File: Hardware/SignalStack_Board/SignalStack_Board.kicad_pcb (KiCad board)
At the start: 2 copper layers, 101.6 x 76.2 mm, 68 parts, among them J1 Molex_uF_SV_06, J2 RJ45_LED_Shielded, J3 Molex_uF_SV_06, Q1 SI4156DY, Q2 SI4156DY, Q3 SI4156DY, Q4 SI4156DY, Q5 SI4156DY, Q6 SI4156DY, Q7 SI4156DY, Q8 SI4156DY, U1 OKI, U10 74LVC2G04, U2 SMAJ12CA, U3 Teensy4.1_DEV-16771, U4 TSR_1-2450, U5 IRS2005S, U6 IRS2005S, U7 74LVC2G04, U8 IRS2005S, U9 IRS2005S

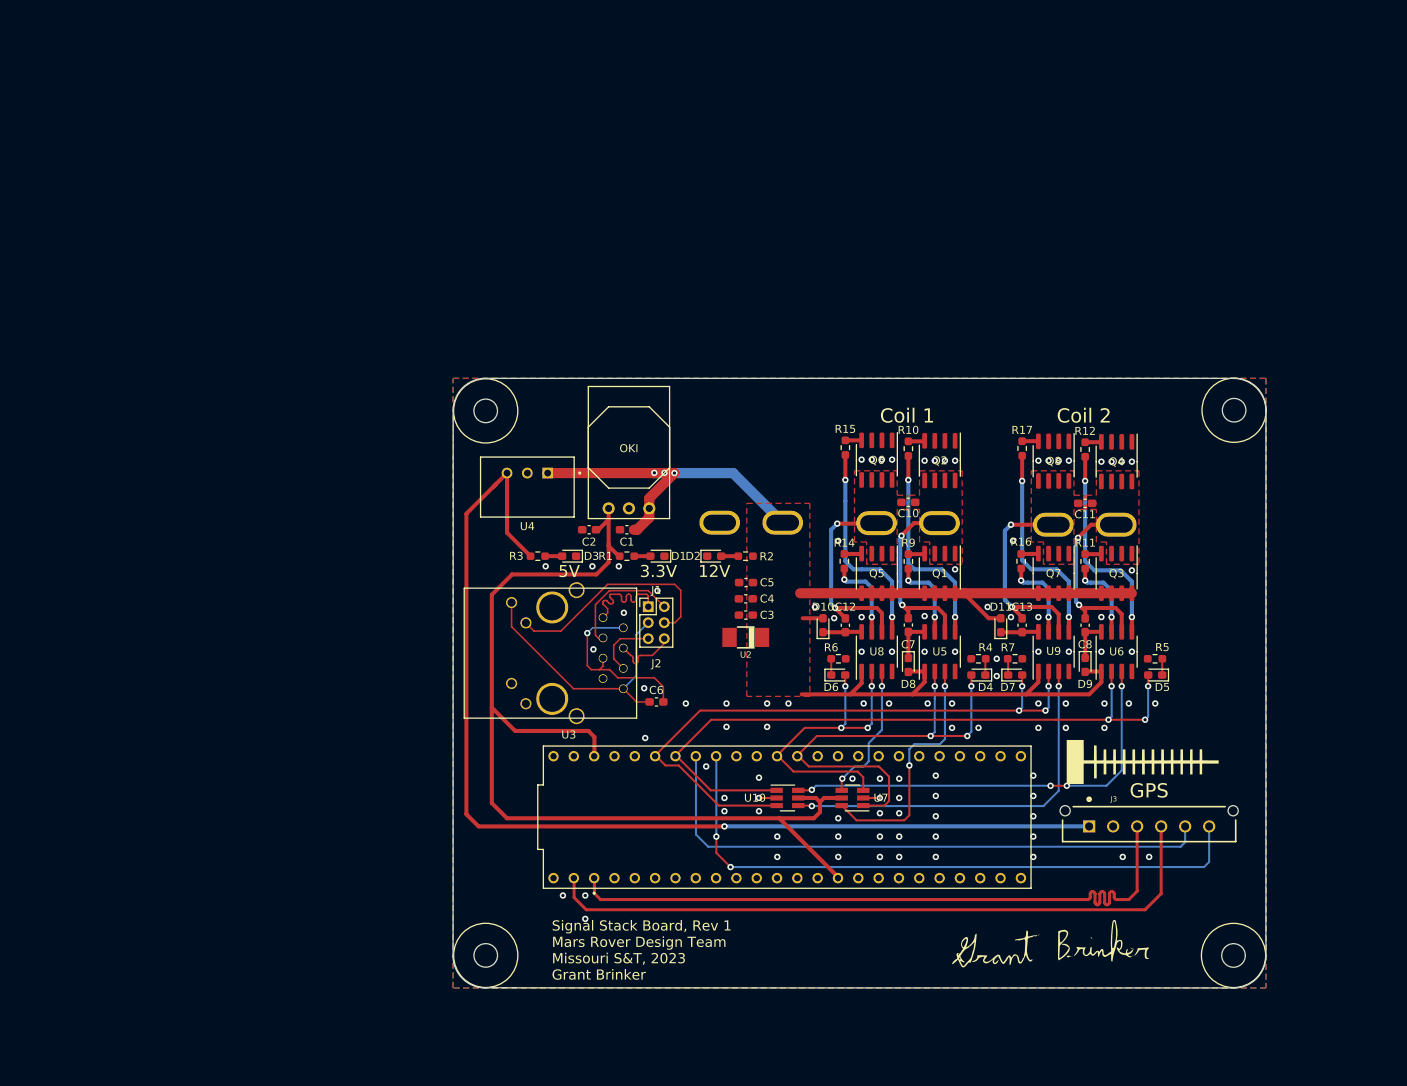
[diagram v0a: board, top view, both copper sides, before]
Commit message: Started layout
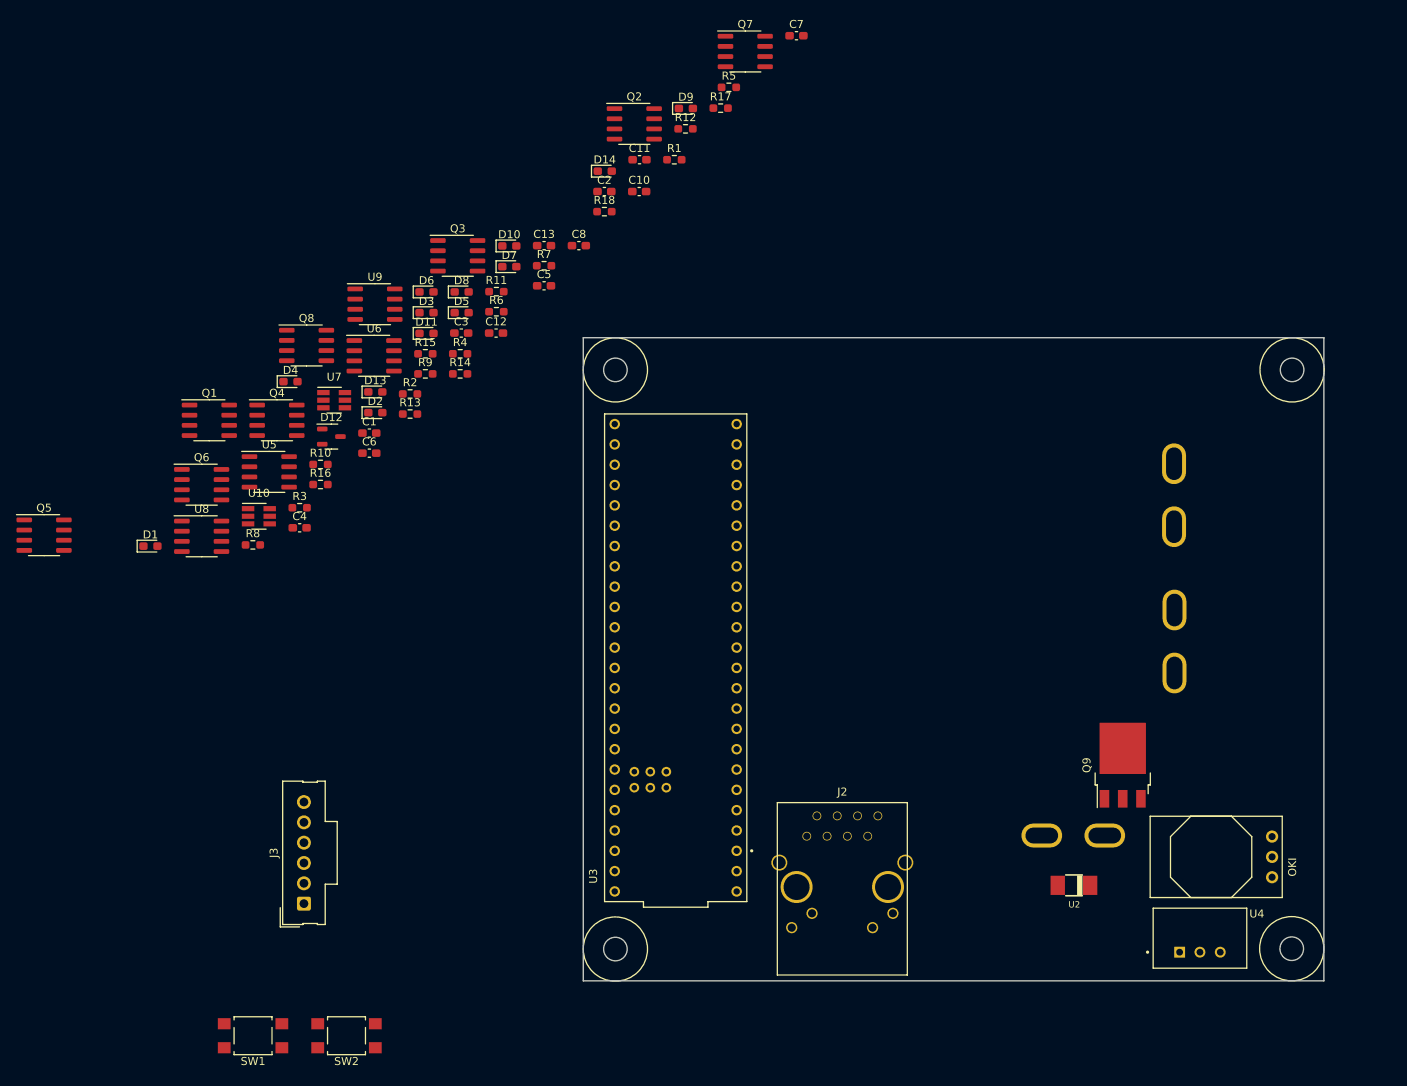
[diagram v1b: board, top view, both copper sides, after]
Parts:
- removed G***: LOGO, MRDT_Silkscreens:yagi
- removed G***: LOGO, MRDT_Silkscreens:z_sig_Grant_Brinker_25mmx6
- removed J1: Molex_uF_SV_06, Connector_PinHeader_2.00mm:PinHeader_2x03_P2.00mm_Vertical
- added D12: D_Zener, Package_TO_SOT_SMD:SOT-23-3, F.Cu at (80.9, 70.4)
- added D13: Blue, LED_SMD:LED_0603_1608Metric_Pad1.05x0.95mm_HandSolder, F.Cu at (86.4, 64.8)
- added D14: Blue, LED_SMD:LED_0603_1608Metric_Pad1.05x0.95mm_HandSolder, F.Cu at (115.1, 37.2)
- added Q9: Q_PMOS_DGS, Package_TO_SOT_SMD:TO-252-3_TabPin2, F.Cu at (179.8, 111.5)
- added R13: 120, Resistor_SMD:R_0603_1608Metric_Pad0.98x0.95mm_HandSolder, F.Cu at (90.8, 67.6)
- added R18: 120, Resistor_SMD:R_0603_1608Metric_Pad0.98x0.95mm_HandSolder, F.Cu at (115.0, 42.3)
- added R8: 100k, Resistor_SMD:R_0603_1608Metric_Pad0.98x0.95mm_HandSolder, F.Cu at (71.1, 83.9)
- added SW1: SW_Push, Button_Switch_SMD:SW_SPST_TL3305A, F.Cu at (71.1, 145.3)
- added SW2: SW_Push, Button_Switch_SMD:SW_SPST_TL3305A, F.Cu at (82.8, 145.3)
- Conn1: moved to F.Cu
- Conn2, Conn3: moved to B.Cu
- J3: footprint MRDT_Connectors:MOLEX_uF_S_06_Vertical -> Connector_Molex:Molex_SL_171971-0006_1x06_P2.54mm_Vertical
- U3: footprint MRDT_Shields:Teensy_4_1_Bare -> MRDT_Shields:Teensy_4_1_Ethernet
- moved V3 108.8 mm to (205.0, 138.4), turned to 90 degrees
- moved J3 106.1 mm to (77.5, 128.8), turned to 90 degrees
- moved Q4 105.1 mm to (74.1, 68.4), turned to 0 degrees
- moved Q5 104.2 mm to (45.0, 82.7), turned to 0 degrees
- moved V1 102.6 mm to (112.4, 138.5)
- moved U4 101.2 mm to (189.5, 133.1), turned to 0 degrees
- moved U6 99.9 mm to (86.3, 60.3), turned to 0 degrees
- moved D5 97.8 mm to (97.2, 54.9), turned to 0 degrees
- moved U9 95.3 mm to (86.4, 53.8), turned to 0 degrees
- moved Q8 94.5 mm to (77.8, 59.0), turned to 0 degrees
- moved D4 93.5 mm to (75.8, 63.5), turned to 0 degrees
- moved Q1 93.3 mm to (65.7, 68.4), turned to 0 degrees
- moved Q3 91.4 mm to (96.7, 47.8), turned to 0 degrees
- moved R5 89.1 mm to (130.6, 26.7)
- moved R16 88.1 mm to (79.5, 76.4), turned to 0 degrees
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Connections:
- C6 pad 2: Net-(C6-Pad2) -> GND
- Conn1 pad 2: +12V -> Net-(Conn1-Pad2)
- J2 pad 10: Net-(J1-Pad4) -> /LED
- J2 pad 8: Net-(C6-Pad2) -> GND
- J2 pad 9: Net-(C6-Pad2) -> GND
- U3 pad 20: Coil2_FWD -> unconnected-(U3-Pad20)
- U3 pad 21: Coil2_RVS -> unconnected-(U3-Pad21)
- U3 pad 22: unconnected-(U3-Pad22) -> Coil2_FWD
- U3 pad 23: unconnected-(U3-Pad23) -> Coil2_RVS
- U3 pad 24: unconnected-(U3-Pad24) -> Motor 1
- U3 pad 25: unconnected-(U3-Pad25) -> Motor 2
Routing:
- net +12V: track 148.8 -> 0.00 mm, vias 3 -> 0
- net +5V: track 135.4 -> 0.00 mm, vias 1 -> 0
- net +3V3: track 129.4 -> 0.00 mm
- net Coil2_FWD: track 86.9 -> 0.00 mm, vias 4 -> 0
- net GPS RX: track 85.8 -> 0.00 mm
- net GPS TX: track 85.6 -> 0.00 mm
- net I2C SDA: track 79.6 -> 0.00 mm, vias 2 -> 0
- net Coil2_RVS: track 78.5 -> 0.00 mm, vias 4 -> 0
- net I2C SCL: track 73.9 -> 0.00 mm
- net Coil1_FWD: track 57.4 -> 0.00 mm, vias 4 -> 0
- net Net-(U10-Pad6): track 53.8 -> 0.00 mm, vias 4 -> 0
- net Net-(U10-Pad4): track 48.3 -> 0.00 mm, vias 2 -> 0
- net Coil1_RVS: track 40.3 -> 0.00 mm, vias 4 -> 0
- net Net-(C6-Pad2): track 33.7 -> 0.00 mm
- net Net-(U5-Pad3): track 31.2 -> 0.00 mm, vias 2 -> 0
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- removed copper zone on F.Cu, net +12V
- removed copper zone on F.Cu, net /M1+
- removed copper zone on F.Cu, net /M1-
- removed copper zone on F.Cu, net /M2+
- removed copper zone on F.Cu, net /M2-
- removed copper zone on B.Cu, net GND
- removed copper zone on F.Cu, net GND
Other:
- board size 101.6 x 76.2 mm -> 92.6 x 80.4 mm
- board text removed: "12V"
- board text removed: "3.3V"
- board text removed: "5V"
- board text removed: "Coil 1"
- board text removed: "Coil 2"
- board text removed: "GPS"
- board text removed: "Signal Stack Board, Rev 1 Mars Rover Design Team Missouri S&T, 2023 Grant Brinker"
- board text removed: "Super Spicy Signal Stack Spinning System"

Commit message: Worked on planes
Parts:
- moved Q5 149.9 mm to (194.0, 99.6)
- moved R3 142.8 mm to (211.9, 126.0)
- moved Q1 130.4 mm to (194.0, 91.7)
- moved Q6 117.1 mm to (179.5, 99.6)
- moved D12 113.3 mm to (186.2, 112.3), turned to 180 degrees
- moved SW1 112.5 mm to (148.1, 63.2), turned to 0 degrees
- moved SW2 112.5 mm to (159.8, 63.2), turned to 0 degrees
- moved C4 109.2 mm to (173.6, 132.6), turned to 180 degrees
- moved C5 106.4 mm to (173.6, 134.9), turned to 180 degrees
- moved C3 105.6 mm to (173.6, 130.3), turned to 180 degrees
- moved Q4 105.5 mm to (179.5, 73.4)
- moved U8 104.7 mm to (168.1, 99.6)
- moved Q8 104.1 mm to (179.5, 81.3)
- moved Q3 100.6 mm to (194.0, 73.4)
- moved U5 96.4 mm to (168.1, 91.7)
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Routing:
- added copper zone on F.Cu, net +12V
- added copper zone on F.Cu, net /M1+
- added copper zone on F.Cu, net /M1-
- added copper zone on F.Cu, net /M2+
- added copper zone on F.Cu, net /M2-
- added copper zone on B.Cu, net GND
- added copper zone on F.Cu, net GND

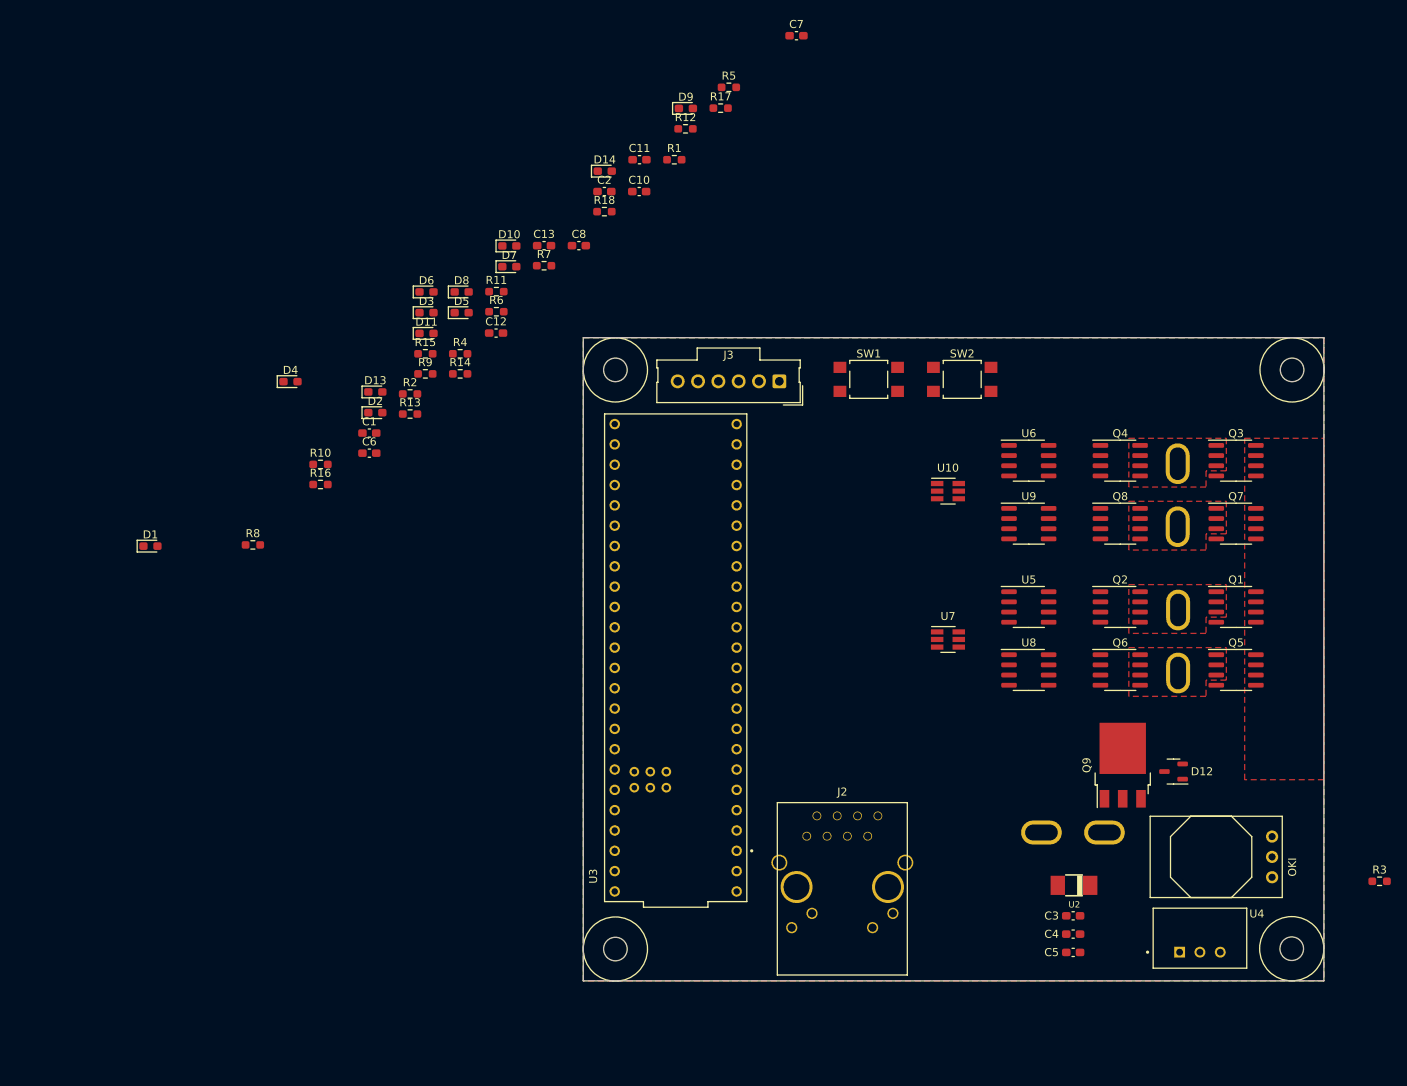
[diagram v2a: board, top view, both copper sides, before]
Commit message: Mostly finished H bridges
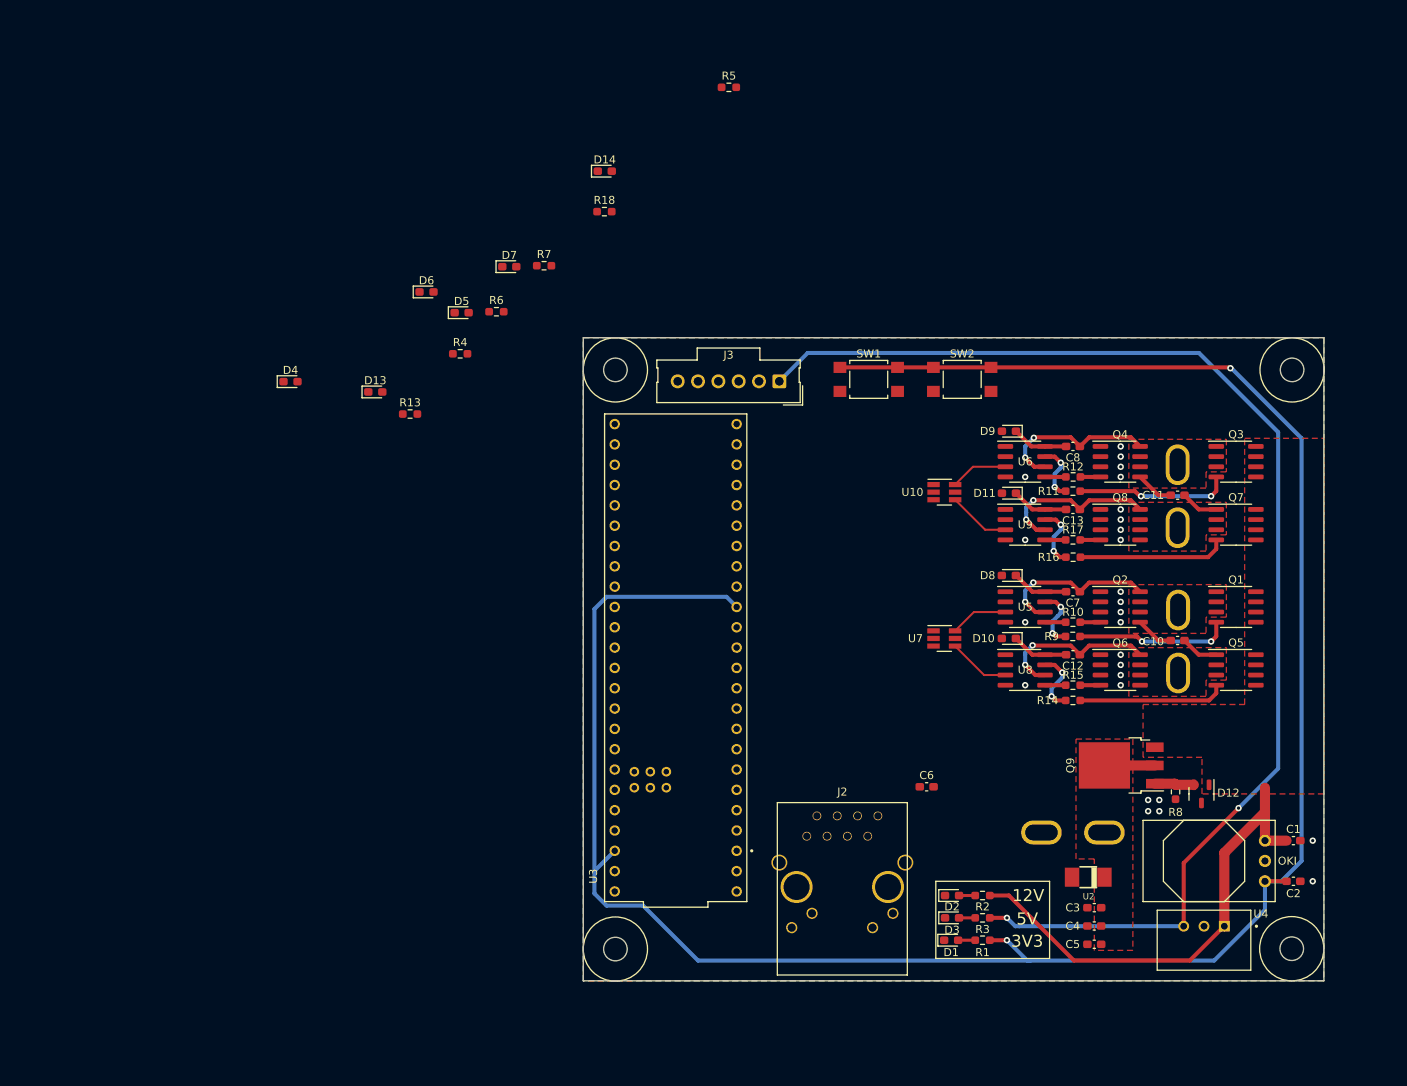
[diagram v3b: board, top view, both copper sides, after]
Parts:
- moved C1 126.2 mm to (201.2, 120.9)
- moved C2 121.9 mm to (201.2, 126.0)
- moved R8 119.4 mm to (186.4, 114.8), turned to 90 degrees
- moved D1 111.6 mm to (158.4, 133.3)
- moved R1 104.9 mm to (162.3, 133.3), turned to 180 degrees
- moved D3 100.2 mm to (158.5, 130.6)
- moved R10 96.1 mm to (173.6, 93.6)
- moved R2 95.1 mm to (162.3, 127.8)
- moved R16 94.5 mm to (173.6, 85.5)
- moved D2 94.0 mm to (158.5, 127.8)
- moved R15 90.9 mm to (173.6, 101.5)
- moved C10 87.6 mm to (186.7, 95.9)
- moved R9 87.3 mm to (173.6, 95.4)
- moved R14 86.8 mm to (173.6, 103.4)
- moved C12 82.6 mm to (173.6, 97.7)
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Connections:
- C3 pad 1: +12V -> Net-(C3-Pad1)
- C4 pad 1: +12V -> Net-(C3-Pad1)
- C5 pad 1: +12V -> Net-(C3-Pad1)
- Conn1 pad 2: Net-(Conn1-Pad2) -> Net-(C3-Pad1)
- Q9 pad 1: Net-(Conn1-Pad2) -> Net-(D12-Pad2)
- Q9 pad 2: Net-(D12-Pad2) -> Net-(C3-Pad1)
- U2 pad C: +12V -> Net-(C3-Pad1)
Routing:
- net +3V3: track 0.00 -> 280.2 mm, vias 0 -> 2
- net +5V: track 0.00 -> 159.2 mm, vias 0 -> 2
- net +12V: track 0.00 -> 60.1 mm
- net /M1-: track 0.00 -> 25.4 mm, vias 0 -> 2
- net /M2+: track 0.00 -> 25.4 mm, vias 0 -> 2
- net /M1+: track 0.00 -> 25.4 mm, vias 0 -> 2
- net /M2-: track 0.00 -> 25.1 mm, vias 0 -> 2
- net Net-(Q1-Pad4): track 0.00 -> 19.3 mm, vias 0 -> 2
- net Net-(Q3-Pad4): track 0.00 -> 19.3 mm, vias 0 -> 2
- net Net-(Q7-Pad4): track 0.00 -> 18.5 mm
- net Net-(Q5-Pad4): track 0.00 -> 18.4 mm
- net Net-(R14-Pad1): track 0.00 -> 8.11 mm, vias 0 -> 2
- net Net-(U10-Pad4): track 0.00 -> 7.83 mm
- net Net-(U7-Pad4): track 0.00 -> 7.79 mm
- net Net-(R16-Pad1): track 0.00 -> 7.74 mm, vias 0 -> 2
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- added copper zone on F.Cu, net Net-(C3-Pad1)
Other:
- board text added: "12V"
- board text added: "3V3"
- board text added: "5V"

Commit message: Finished layout
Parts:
- added G***: LOGO, MRDT_Silkscreens:0_MRDT_Logo_20mm, F.Cu at (143.8, 104.6)
- added G***: LOGO, MRDT_Silkscreens:z_sig_Grant_Brinker_25mmx6, F.Cu at (183.6, 64.5)
- moved D4 85.2 mm to (156.2, 91.6), turned to -90 degrees
- moved D6 79.1 mm to (156.2, 99.7), turned to 90 degrees
- moved R6 69.2 mm to (154.2, 99.7), turned to -90 degrees
- moved R4 65.3 mm to (154.2, 91.6), turned to 90 degrees
- moved D7 62.1 mm to (156.2, 81.4), turned to 90 degrees
- moved D5 61.8 mm to (156.2, 73.4), turned to -90 degrees
- moved D14 57.3 mm to (136.9, 90.2), turned to 180 degrees
- moved R7 56.8 mm to (154.2, 81.4), turned to -90 degrees
- moved R18 54.5 mm to (136.9, 92.2), turned to 180 degrees
- moved D13 53.3 mm to (136.9, 81.8), turned to 180 degrees
- moved R5 52.3 mm to (154.2, 73.4), turned to 90 degrees
- moved R13 48.9 mm to (136.9, 83.8), turned to 180 degrees
- moved SW2 31.8 mm to (143.8, 90.7)
- moved SW1 19.5 mm to (143.8, 82.3)
- moved C6 6.54 mm to (148.8, 113.3)
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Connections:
- U3 pad 0: GPS RX -> unconnected-(U3-Pad0)
- U3 pad 1: GPS TX -> unconnected-(U3-Pad1)
- U3 pad 11: unconnected-(U3-Pad11) -> Coil1_RVS
- U3 pad 12: unconnected-(U3-Pad12) -> Coil1_FWD
- U3 pad 14: Coil1_FWD -> unconnected-(U3-Pad14)
- U3 pad 15: Coil1_RVS -> unconnected-(U3-Pad15)
- U3 pad 22: Coil2_FWD -> unconnected-(U3-Pad22)
- U3 pad 23: Coil2_RVS -> unconnected-(U3-Pad23)
- U3 pad 28: unconnected-(U3-Pad28) -> Coil2_RVS
- U3 pad 29: unconnected-(U3-Pad29) -> Coil2_FWD
- U3 pad 34: unconnected-(U3-Pad34) -> GPS RX
- U3 pad 35: unconnected-(U3-Pad35) -> GPS TX
- U3 pad R-: (no net) -> /RX-
- U3 pad T-: (no net) -> /TX-
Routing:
- net +12V: track 60.1 -> 119.3 mm
- net I2C SCL: track 0.00 -> 50.3 mm
- net I2C SDA: track 0.00 -> 46.7 mm
- net Coil1_FWD: track 0.00 -> 40.5 mm, vias 0 -> 2
- net Coil2_FWD: track 0.00 -> 40.0 mm, vias 0 -> 2
- net Coil2_RVS: track 0.00 -> 40.0 mm, vias 0 -> 2
- net Coil1_RVS: track 0.00 -> 39.6 mm, vias 0 -> 2
- net /RX-: track 0.00 -> 38.2 mm
- net /RX+: track 0.00 -> 38.0 mm
- net /LED: track 0.00 -> 33.1 mm
- net /TX+: track 0.00 -> 26.9 mm
- net /TX-: track 0.00 -> 26.9 mm
- net Motor 1: track 0.00 -> 20.9 mm
- net GPS TX: track 0.00 -> 19.8 mm
- net Motor 2: track 0.00 -> 19.3 mm
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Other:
- outline, holes or cut-outs redrawn
- board text added: "Signal Stack Board, Rev 2 Mars Rover Design Team Missouri S&T, 2023 Grant Brinker"
